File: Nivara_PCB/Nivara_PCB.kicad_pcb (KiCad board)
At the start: 4 copper layers, 102.2 x 83 mm, 14 parts, among them J1 NPN_IN, J10 Analog_Out, J11 RELAY, J2 PNP_IN, J3 D_IN, J4 Analaog_In, J5 RUN/STOP, J6 FUENTE, J7 NPN_OUT, J8 PNP_OUT, J9 RS485, U1 ESP32-S3-WROOM-1

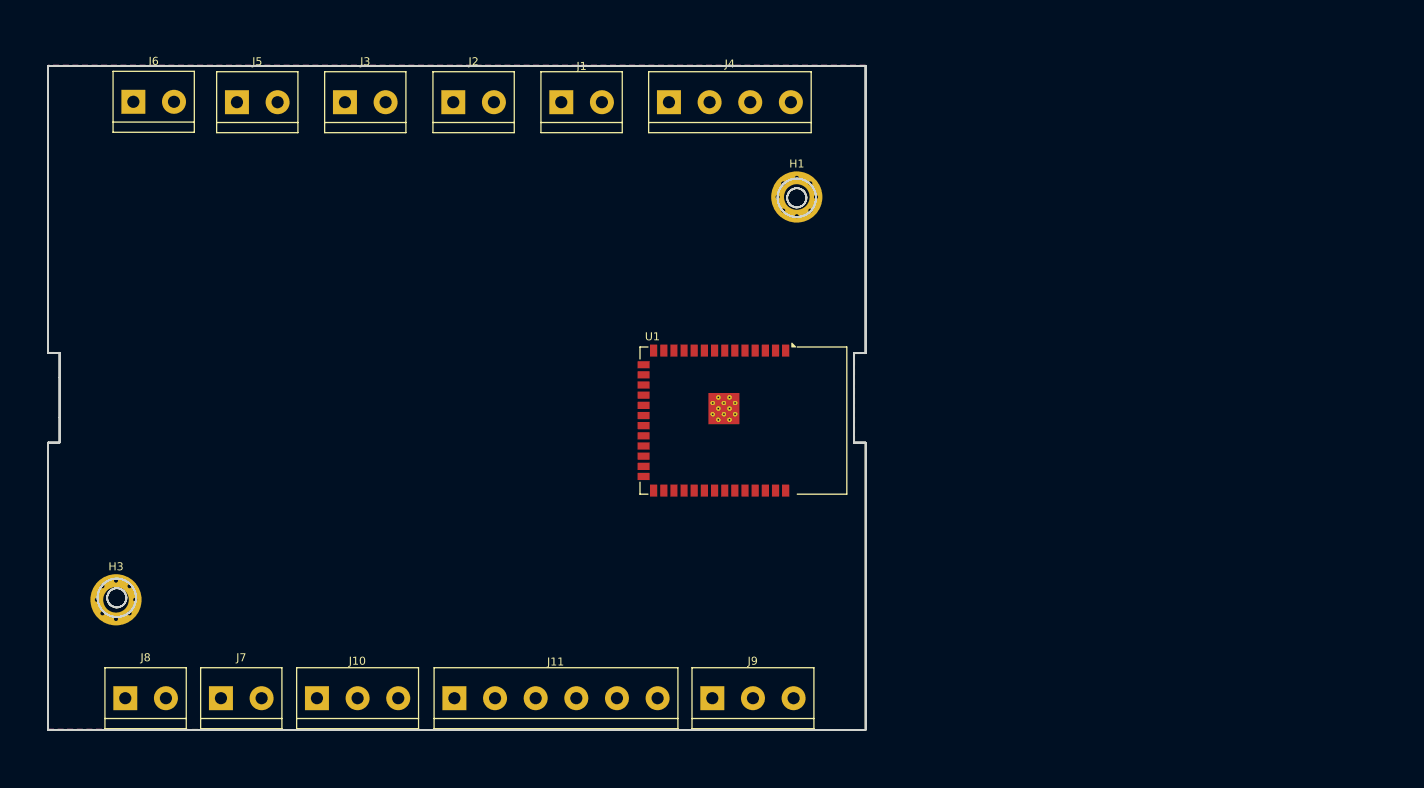
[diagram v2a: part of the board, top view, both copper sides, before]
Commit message: Cambios en el PCB de Nivara. Ruteo de emtradas y salidas NPN y PNP.
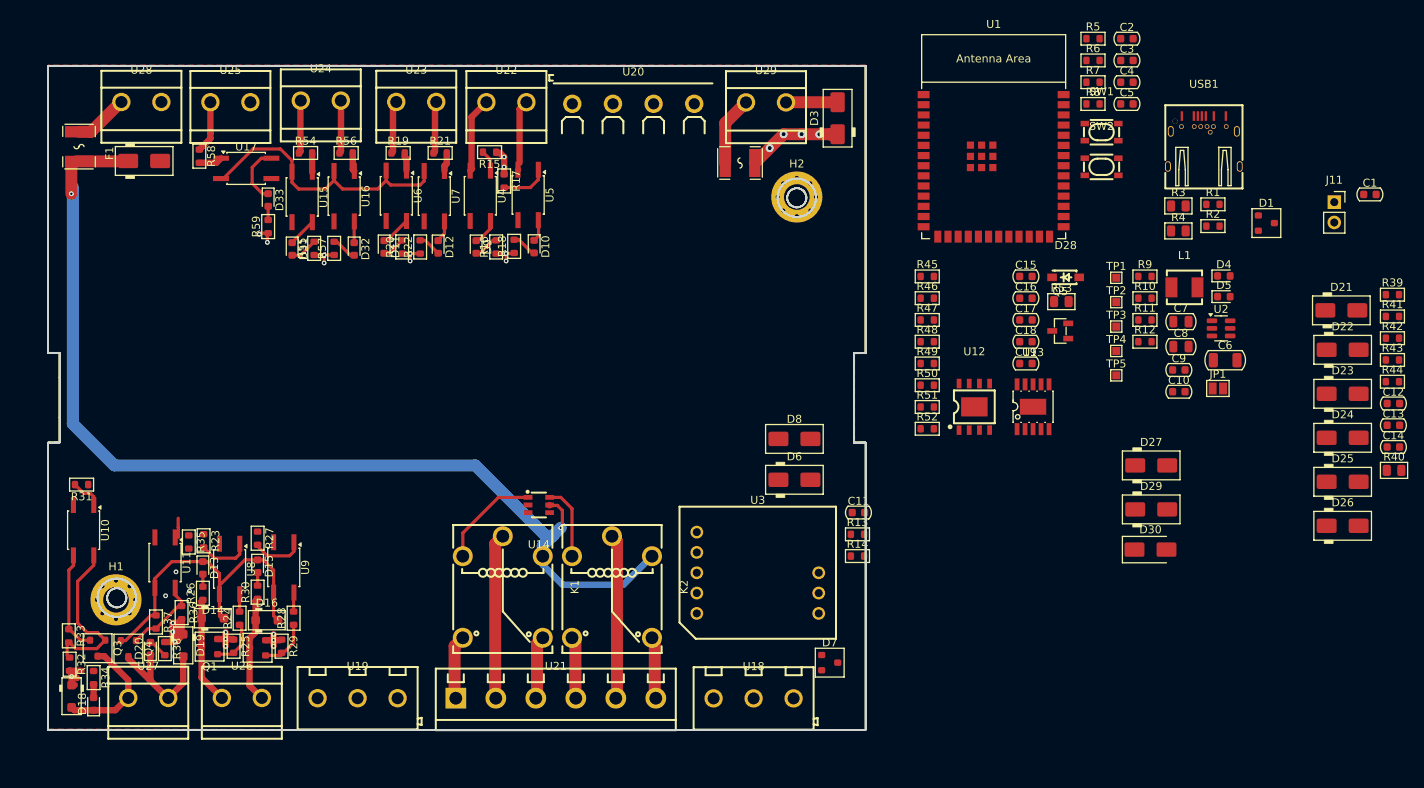
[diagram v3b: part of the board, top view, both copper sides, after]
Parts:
- removed J1: NPN_IN, TerminalBlock:TerminalBlock_bornier-2_P5.08mm
- removed J10: Analog_Out, TerminalBlock:TerminalBlock_bornier-3_P5.08mm
- removed J2: PNP_IN, TerminalBlock:TerminalBlock_bornier-2_P5.08mm
- removed J3: D_IN, TerminalBlock:TerminalBlock_bornier-2_P5.08mm
- removed J4: Analaog_In, TerminalBlock:TerminalBlock_bornier-4_P5.08mm
- removed J5: RUN/STOP, TerminalBlock:TerminalBlock_bornier-2_P5.08mm
- removed J6: FUENTE, TerminalBlock:TerminalBlock_bornier-2_P5.08mm
- removed J7: NPN_OUT, TerminalBlock:TerminalBlock_bornier-2_P5.08mm
- removed J8: PNP_OUT, TerminalBlock:TerminalBlock_bornier-2_P5.08mm
- removed J9: RS485, TerminalBlock:TerminalBlock_bornier-3_P5.08mm
- added C1: 100nF, PCM_Capacitor_SMD_AKL:C_0603_1608Metric, F.Cu at (263.5, 61.0)
- added C10: 22uF, PCM_Capacitor_SMD_AKL:C_0603_1608Metric, F.Cu at (239.7, 85.7)
- added C11: 10uF, PCM_Capacitor_SMD_AKL:C_0603_1608Metric, F.Cu at (199.6, 100.8)
- added C12: 10nF, PCM_Capacitor_SMD_AKL:C_0603_1608Metric, F.Cu at (266.5, 87.2)
- added C13: 100nF, PCM_Capacitor_SMD_AKL:C_0603_1608Metric, F.Cu at (266.5, 89.9)
- added C14: 100nF, PCM_Capacitor_SMD_AKL:C_0603_1608Metric, F.Cu at (266.5, 92.6)
- added C15: 0.1uF, PCM_Capacitor_SMD_AKL:C_0603_1608Metric, F.Cu at (220.5, 71.3)
- added C16: 1uF, PCM_Capacitor_SMD_AKL:C_0603_1608Metric, F.Cu at (220.5, 74.0)
- added C17: 220pF, PCM_Capacitor_SMD_AKL:C_0603_1608Metric, F.Cu at (220.5, 76.7)
- added C18: 1uF, PCM_Capacitor_SMD_AKL:C_0603_1608Metric, F.Cu at (220.5, 79.4)
- added C19: 0.1uF, PCM_Capacitor_SMD_AKL:C_0603_1608Metric, F.Cu at (220.5, 82.2)
- added C2: 22uF, PCM_Capacitor_SMD_AKL:C_0603_1608Metric, F.Cu at (233.2, 41.6)
- added C3: 1uF, PCM_Capacitor_SMD_AKL:C_0603_1608Metric, F.Cu at (233.2, 44.3)
- added C4: 100nF, PCM_Capacitor_SMD_AKL:C_0603_1608Metric, F.Cu at (233.2, 47.0)
- added C5: 1uF, PCM_Capacitor_SMD_AKL:C_0603_1608Metric, F.Cu at (233.2, 49.7)
- added C6: 10uF, PCM_Capacitor_SMD_AKL:C_1206_3216Metric, F.Cu at (245.4, 81.8)
- added C7: 100nF, PCM_Capacitor_SMD_AKL:C_0805_2012Metric, F.Cu at (239.9, 76.9)
- added C8: 100pF, PCM_Capacitor_SMD_AKL:C_0805_2012Metric, F.Cu at (239.9, 80.0)
- added C9: 22uF, PCM_Capacitor_SMD_AKL:C_0603_1608Metric, F.Cu at (239.7, 83.0)
- added D1: SM712, PCM_Package_TO_SOT_SMD_AKL:SOT-23, F.Cu at (250.6, 64.6)
- added D10: LED ON, LED_SMD:LED_0603_1608Metric, F.Cu at (159.1, 67.6)
- added D11: LED ON, LED_SMD:LED_0603_1608Metric, F.Cu at (140.3, 67.6)
- added D12: LED ON, LED_SMD:LED_0603_1608Metric, F.Cu at (147.1, 67.6)
- added D13: LED ON, LED_SMD:LED_0603_1608Metric, F.Cu at (117.7, 107.7)
- added D14: PMEG4010CEH, PCM_Diode_SMD_AKL:D_SOD-123F, F.Cu at (118.9, 114.0)
- added D15: LED ON, LED_SMD:LED_0603_1608Metric, F.Cu at (124.5, 107.5)
- added D16: PMEG4010CEH, PCM_Diode_SMD_AKL:D_SOD-123F, F.Cu at (125.7, 114.2)
- added D17: PMEG4010CEH, PCM_Diode_SMD_AKL:D_SOD-123F, F.Cu at (101.2, 123.8)
- added D18: LED ON, LED_SMD:LED_0603_1608Metric, F.Cu at (104.0, 124.7)
- added D19: PMEG4010CEH, PCM_Diode_SMD_AKL:D_SOD-123F, F.Cu at (115.2, 117.4)
- added D2: SMAJ33A, PCM_Diode_SMD_AKL:D_SMA, F.Cu at (110.3, 56.8)
- added D20: LED ON, LED_SMD:LED_0603_1608Metric, F.Cu at (111.1, 117.8)
- added D21: SMAJ5.0A, PCM_Diode_SMD_AKL:D_SMA, F.Cu at (260.0, 75.5)
- added D22: SMAJ5.0A, PCM_Diode_SMD_AKL:D_SMA, F.Cu at (260.1, 80.4)
- added D23: SMAJ5.0A, PCM_Diode_SMD_AKL:D_SMA, F.Cu at (260.1, 85.9)
- added D24: SMAJ5.0A, PCM_Diode_SMD_AKL:D_SMA, F.Cu at (260.1, 91.4)
- added D25: SMAJ5.0A, PCM_Diode_SMD_AKL:D_SMA, F.Cu at (260.1, 96.9)
- added D26: SMAJ5.0A, PCM_Diode_SMD_AKL:D_SMA, F.Cu at (260.1, 102.4)
- added D27: SMAJ12A, PCM_Diode_SMD_AKL:D_SMA, F.Cu at (236.2, 94.9)
- added D28: BZT52C12_C2891780, EasyEDA:SOD-123_L2.7-W1.6-LS3.7-RD-1, F.Cu at (225.5, 71.4)
- added D29: SMAJ33A, PCM_Diode_SMD_AKL:D_SMA, F.Cu at (236.2, 100.4)
- added D3: SMAJ33A, PCM_Diode_SMD_AKL:D_SMA, F.Cu at (197.0, 51.5)
- added D30: MRA4007T3G, Diode_SMD:D_SMA, F.Cu at (236.1, 105.4)
- added D31: LED ON, LED_SMD:LED_0603_1608Metric, F.Cu at (128.8, 67.8)
- added D32: LED ON, LED_SMD:LED_0603_1608Metric, F.Cu at (136.6, 67.8)
- added D33: LED ON, LED_SMD:LED_0603_1608Metric, F.Cu at (125.8, 61.7)
- added D4: LED ON, LED_SMD:LED_0603_1608Metric, F.Cu at (245.3, 71.2)
- added D5: LED 3.3V, LED_SMD:LED_0603_1608Metric, F.Cu at (245.3, 73.8)
- added D6: SMAJ5.0A, PCM_Diode_SMD_AKL:D_SMA, F.Cu at (191.6, 96.7)
- added D7: SM712, PCM_Package_TO_SOT_SMD_AKL:SOT-23, F.Cu at (196.0, 119.6)
- added D8: SMAJ12CA, PCM_Diode_SMD_AKL:D_SMA_TVS, F.Cu at (191.6, 91.6)
- added D9: LED ON, LED_SMD:LED_0603_1608Metric, F.Cu at (151.8, 67.6)
- added F1: BSMD1812-150-33V, EasyEDA:F1812, F.Cu at (102.2, 55.0)
- added F2: BSMD1812-150-33V, EasyEDA:F1812, F.Cu at (184.8, 57.1)
- added JP1: SolderJumper_2_Open, Jumper:SolderJumper-2_P1.3mm_Open_Pad1.0x1.5mm, F.Cu at (244.5, 85.3)
- added K1: SRA-24VDC-CL, EasyEDA:RELAY-TH_SRA-X-CX, F.Cu at (155.2, 110.1)
- added K2: SRA-24VDC-CL, EasyEDA:RELAY-TH_SRA-X-CX, F.Cu at (168.8, 110.1)
- added L1: CXP0420-6R8M-AG(6.8UH), EasyEDA:IND-SMD_L4.4-W4.2_CXP0420, F.Cu at (240.4, 72.6)
- added Q1: AO3407A, PCM_Package_TO_SOT_SMD_AKL:SOT-23, F.Cu at (118.5, 117.5)
- added Q2: AO3407A, PCM_Package_TO_SOT_SMD_AKL:SOT-23, F.Cu at (124.5, 117.7)
- added Q3: IRLML0040, PCM_Package_TO_SOT_SMD_AKL:SOT-23, F.Cu at (104.5, 117.8)
- added Q4: IRLML0040, PCM_Package_TO_SOT_SMD_AKL:SOT-23, F.Cu at (108.3, 117.8)
- added Q5: IRLML6402TRPBF-JSM, EasyEDA:SOT-23-3_L2.9-W1.3-P1.90-LS2.4-BR, F.Cu at (224.8, 78.1)
- added R1: 14k, PCM_Resistor_SMD_AKL:R_0603_1608Metric, F.Cu at (243.9, 62.3)
- added R10: 196k, PCM_Resistor_SMD_AKL:R_0603_1608Metric, F.Cu at (235.4, 74.0)
- added R11: 62k, PCM_Resistor_SMD_AKL:R_0603_1608Metric, F.Cu at (235.4, 76.7)
- added R12: 100, PCM_Resistor_SMD_AKL:R_0603_1608Metric, F.Cu at (235.4, 79.4)
- added R13: R_0603, PCM_Resistor_SMD_AKL:R_0603_1608Metric, F.Cu at (199.5, 103.5)
- added R14: R_0603, PCM_Resistor_SMD_AKL:R_0603_1608Metric, F.Cu at (199.5, 106.2)
- added R15: 1k, PCM_Resistor_SMD_AKL:R_0603_1608Metric, F.Cu at (153.5, 55.7)
- added R16: 140, PCM_Resistor_SMD_AKL:R_0603_1608Metric, F.Cu at (154.3, 67.6)
- added R17: 1k, PCM_Resistor_SMD_AKL:R_0603_1608Metric, F.Cu at (155.3, 59.3)
- added R18: 140, PCM_Resistor_SMD_AKL:R_0603_1608Metric, F.Cu at (156.6, 67.5)
- added R19: 1k, PCM_Resistor_SMD_AKL:R_0603_1608Metric, F.Cu at (142.1, 55.8)
- added R2: 10k, PCM_Resistor_SMD_AKL:R_0603_1608Metric, F.Cu at (243.9, 65.0)
- added R20: 140, PCM_Resistor_SMD_AKL:R_0603_1608Metric, F.Cu at (142.6, 67.6)
- added R21: 1k, PCM_Resistor_SMD_AKL:R_0603_1608Metric, F.Cu at (147.3, 55.8)
- added R22: 140, PCM_Resistor_SMD_AKL:R_0603_1608Metric, F.Cu at (144.8, 67.6)
- added R23: 100, PCM_Resistor_SMD_AKL:R_0603_1608Metric, F.Cu at (117.8, 104.3)
- added R24: 100, PCM_Resistor_SMD_AKL:R_0603_1608Metric, F.Cu at (122.2, 114.0)
- added R25: 100k, PCM_Resistor_SMD_AKL:R_0603_1608Metric, F.Cu at (121.5, 117.5)
- added R26: 1.5k, PCM_Resistor_SMD_AKL:R_0603_1608Metric, F.Cu at (117.7, 110.9)
- added R27: 100, PCM_Resistor_SMD_AKL:R_0603_1608Metric, F.Cu at (124.5, 104.0)
- added R28: 100, PCM_Resistor_SMD_AKL:R_0603_1608Metric, F.Cu at (129.0, 114.0)
- added R29: 100k, PCM_Resistor_SMD_AKL:R_0603_1608Metric, F.Cu at (127.5, 117.5)
- added R3: 5.1k, PCM_Resistor_SMD_AKL:R_0805_2012Metric, F.Cu at (239.6, 62.5)
- added R30: 1.5k, PCM_Resistor_SMD_AKL:R_0603_1608Metric, F.Cu at (124.5, 110.8)
- added R31: 100, PCM_Resistor_SMD_AKL:R_0603_1608Metric, F.Cu at (102.5, 97.3)
- added R32: 30k, PCM_Resistor_SMD_AKL:R_0603_1608Metric, F.Cu at (101.0, 119.8)
- added R33: 22k, PCM_Resistor_SMD_AKL:R_0603_1608Metric, F.Cu at (100.9, 116.2)
- added R34: 1.5k, PCM_Resistor_SMD_AKL:R_0603_1608Metric, F.Cu at (104.0, 121.4)
- added R35: 100, PCM_Resistor_SMD_AKL:R_0603_1608Metric, F.Cu at (115.9, 104.5)
- added R36: 30k, PCM_Resistor_SMD_AKL:R_0603_1608Metric, F.Cu at (115.0, 113.3)
- added R37: 22k, PCM_Resistor_SMD_AKL:R_0603_1608Metric, F.Cu at (111.8, 114.5)
- added R38: 1.5k, PCM_Resistor_SMD_AKL:R_0603_1608Metric, F.Cu at (112.9, 117.8)
- added R39: 1k, PCM_Resistor_SMD_AKL:R_0603_1608Metric, F.Cu at (266.4, 73.6)
- added R4: 5.1k, PCM_Resistor_SMD_AKL:R_0805_2012Metric, F.Cu at (239.6, 65.6)
- added R40: 145, PCM_Resistor_SMD_AKL:R_0805_2012Metric, F.Cu at (266.6, 95.5)
- added R41: 100k, PCM_Resistor_SMD_AKL:R_0603_1608Metric, F.Cu at (266.4, 76.3)
- added R42: 10k, PCM_Resistor_SMD_AKL:R_0603_1608Metric, F.Cu at (266.4, 79.0)
- added R43: 24k, PCM_Resistor_SMD_AKL:R_0603_1608Metric, F.Cu at (266.4, 81.7)
- added R44: 10k, PCM_Resistor_SMD_AKL:R_0603_1608Metric, F.Cu at (266.4, 84.4)
- added R45: 4K7, PCM_Resistor_SMD_AKL:R_0603_1608Metric, F.Cu at (208.2, 71.3)
- added R46: 4K7, PCM_Resistor_SMD_AKL:R_0603_1608Metric, F.Cu at (208.2, 74.0)
- added R47: 0, PCM_Resistor_SMD_AKL:R_0603_1608Metric, F.Cu at (208.2, 76.7)
- added R48: 10K, PCM_Resistor_SMD_AKL:R_0603_1608Metric, F.Cu at (208.2, 79.4)
- added R49: 4K7, PCM_Resistor_SMD_AKL:R_0603_1608Metric, F.Cu at (208.2, 82.2)
- added R5: 10k, PCM_Resistor_SMD_AKL:R_0603_1608Metric, F.Cu at (228.9, 41.6)
- added R50: 4K7, PCM_Resistor_SMD_AKL:R_0603_1608Metric, F.Cu at (208.2, 84.9)
- added R51: 2.5k, PCM_Resistor_SMD_AKL:R_0603_1608Metric, F.Cu at (208.2, 87.6)
- added R52: 100k, PCM_Resistor_SMD_AKL:R_0603_1608Metric, F.Cu at (208.2, 90.3)
- added R53: 15, PCM_Resistor_SMD_AKL:R_0805_2012Metric, F.Cu at (225.0, 74.4)
- added R54: 1k, PCM_Resistor_SMD_AKL:R_0603_1608Metric, F.Cu at (130.5, 55.8)
- added R55: 140, PCM_Resistor_SMD_AKL:R_0603_1608Metric, F.Cu at (131.6, 67.8)
- added R56: 1k, PCM_Resistor_SMD_AKL:R_0603_1608Metric, F.Cu at (135.6, 55.8)
- added R57: 140, PCM_Resistor_SMD_AKL:R_0603_1608Metric, F.Cu at (134.1, 67.8)
- added R58: 1k, PCM_Resistor_SMD_AKL:R_0603_1608Metric, F.Cu at (117.2, 56.2)
- added R59: 140, PCM_Resistor_SMD_AKL:R_0603_1608Metric, F.Cu at (125.8, 65.0)
- added R6: 220, PCM_Resistor_SMD_AKL:R_0603_1608Metric, F.Cu at (228.9, 44.3)
- added R7: 220, PCM_Resistor_SMD_AKL:R_0603_1608Metric, F.Cu at (228.9, 47.0)
- added R8: 10k, PCM_Resistor_SMD_AKL:R_0603_1608Metric, F.Cu at (228.9, 49.7)
- added R9: 1k2, PCM_Resistor_SMD_AKL:R_0603_1608Metric, F.Cu at (235.4, 71.3)
- added SW1: SKRPACE010, EasyEDA:KEY-SMD_4P-L4.2-W3.2-P2.20-LS4.6, F.Cu at (230.0, 53.2)
- added SW2: SKRPACE010, EasyEDA:KEY-SMD_4P-L4.2-W3.2-P2.20-LS4.6, F.Cu at (230.0, 57.6)
- added TP1: +VCC1, TestPoint:TestPoint_Pad_1.0x1.0mm, F.Cu at (231.8, 71.4)
- added TP2: FB, TestPoint:TestPoint_Pad_1.0x1.0mm, F.Cu at (231.8, 74.5)
- added TP3: GND, TestPoint:TestPoint_Pad_1.0x1.0mm, F.Cu at (231.8, 77.5)
- added TP4: +3.3V, TestPoint:TestPoint_Pad_1.0x1.0mm, F.Cu at (231.8, 80.6)
- added TP5: +3.3Vout, TestPoint:TestPoint_Pad_1.0x1.0mm, F.Cu at (231.8, 83.6)
- added U10: LTV-357T, Package_SO:SO-4_4.4x3.6mm_P2.54mm, F.Cu at (102.8, 103.0)
- added U11: LTV-357T, Package_SO:SO-4_4.4x3.6mm_P2.54mm, F.Cu at (112.9, 107.0)
- added U12: GP8201S-TC50-EW, EasyEDA:ESOP-8_L4.9-W3.9-P1.27-LS6.0-BL-EP, F.Cu at (214.1, 87.6)
- added U13: GP8303-TC50-EW, EasyEDA:ESOP-10_L4.9-W3.9-P1.00-LS6.1-BL-EP, F.Cu at (221.4, 87.6)
- added U14: LK1802, EasyEDA:SOT-23-6_L2.9-W1.6-P0.95-LS2.8-BR, F.Cu at (159.7, 99.8)
- added U15: LTV-357T, Package_SO:SO-4_4.4x3.6mm_P2.54mm, F.Cu at (130.1, 61.3)
- added U16: LTV-357T, Package_SO:SO-4_4.4x3.6mm_P2.54mm, F.Cu at (135.3, 61.2)
- added U17: LTV-357T, Package_SO:SO-4_4.4x3.6mm_P2.54mm, F.Cu at (123.1, 57.8)
- added U18: RS485, EasyEDA:CONN-TH_XY126V-5.0-3P, F.Cu at (186.5, 124.0)
- added U19: ANALOG_OUT., EasyEDA:CONN-TH_XY126V-5.0-3P, F.Cu at (137.0, 124.0)
- added U2: AP63200WU, Package_TO_SOT_SMD:TSOT-23-6, F.Cu at (244.9, 77.8)
- added U20: ANALOG_IN, EasyEDA:CONN-TH_4P-P5.00_DIBO_DB126V-5.0-4P-GN-P, F.Cu at (171.5, 49.7)
- added U21: RELAY, EasyEDA:CONN-TH_DB126V-5.0-6P-GN, F.Cu at (161.8, 124.0)
- added U22: NPN_IN, EasyEDA:CONN-TH_XY126V-5.0-2P, F.Cu at (155.6, 49.5)
- added U23: PNP_IN, EasyEDA:CONN-TH_XY126V-5.0-2P, F.Cu at (144.3, 49.5)
- added U24: D_IN, EasyEDA:CONN-TH_XY126V-5.0-2P, F.Cu at (132.4, 49.3)
- added U25: RUN/STOP, EasyEDA:CONN-TH_XY126V-5.0-2P, F.Cu at (121.1, 49.5)
- added U26: NPN_OUT, EasyEDA:CONN-TH_XY126V-5.0-2P, F.Cu at (122.5, 124.0)
- added U27: PNP_OUT, EasyEDA:CONN-TH_XY126V-5.0-2P, F.Cu at (110.8, 124.0)
- added U28: FUENTE IN, EasyEDA:CONN-TH_XY126V-5.0-2P, F.Cu at (110.0, 49.5)
- added U29: FUENTE EX, EasyEDA:CONN-TH_XY126V-5.0-2P, F.Cu at (188.1, 49.5)
- added U3: RSM3485ECHT_C2992406, EasyEDA:COMM-TH_8P-L19.5-W16.5-P2.54-BL, F.Cu at (187.0, 108.3)
- added U4: LTV-357T, Package_SO:SO-4_4.4x3.6mm_P2.54mm, F.Cu at (152.3, 61.2)
- added U5: LTV-357T, Package_SO:SO-4_4.4x3.6mm_P2.54mm, F.Cu at (158.3, 61.1)
- added U6: LTV-357T, Package_SO:SO-4_4.4x3.6mm_P2.54mm, F.Cu at (141.8, 61.2)
- added U7: LTV-357T, Package_SO:SO-4_4.4x3.6mm_P2.54mm, F.Cu at (146.6, 61.2)
- added U8: LTV-357T, Package_SO:SO-4_4.4x3.6mm_P2.54mm, F.Cu at (121.0, 107.8)
- added U9: LTV-357T, Package_SO:SO-4_4.4x3.6mm_P2.54mm, F.Cu at (127.8, 107.7)
- added USB1: USB-306B, EasyEDA:USB-TYPE-C-TH_USB-306B, F.Cu at (242.8, 54.4)
- J11: value RELAY -> PINHD_1x2_Female; footprint TerminalBlock:TerminalBlock_bornier-6_P5.08mm -> Connector_PinSocket_2.54mm:PinSocket_1x02_P2.54mm_Vertical
- U1: footprint RF_Module:ESP32-S3-WROOM-1 -> PCM_Espressif:ESP32-S3-WROOM-1
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- renumbered H3 to H1, H1 to H2
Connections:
- net GND renamed GND1
- J11 pad 1: /NIVARA_BOARD/RLY_1_NC -> /NIVARA_BOARD/AUX_1
- J11 pad 2: /NIVARA_BOARD/RLY_1_C -> /NIVARA_BOARD/AUX_2
- U1 pad 13: unconnected-(U1-USB_D--Pad13) -> /NIVARA_BOARD/USB_D-
- U1 pad 14: unconnected-(U1-USB_D+-Pad14) -> /NIVARA_BOARD/USB_D+
- U1 pad 18: unconnected-(U1-IO10-Pad18) -> /NIVARA_BOARD/ANALOG_OUT/ESP_SEL_VOUT
- U1 pad 19: unconnected-(U1-IO11-Pad19) -> /NIVARA_BOARD/ANALOG_OUT/SCLK_V
- U1 pad 20: unconnected-(U1-IO12-Pad20) -> /NIVARA_BOARD/ANALOG_OUT/SDA_V
- U1 pad 21: unconnected-(U1-IO13-Pad21) -> /NIVARA_BOARD/ANALOG_OUT/SCLK_C
- U1 pad 22: unconnected-(U1-IO14-Pad22) -> /NIVARA_BOARD/ANALOG_OUT/SDA_C
- U1 pad 23: unconnected-(U1-IO21-Pad23) -> /NIVARA_BOARD/PNP_OUT/ESP_PNP_OUT_1
- U1 pad 24: unconnected-(U1-IO47-Pad24) -> /NIVARA_BOARD/PNP_OUT/ESP_PNP_OUT_2
- U1 pad 25: unconnected-(U1-IO48-Pad25) -> Net-(U1-GPIO48/SPICLK_N/SUBSPICLK_N_DIFF)
- U1 pad 26: unconnected-(U1-IO45-Pad26) -> Net-(U1-GPIO45)
- U1 pad 27: unconnected-(U1-IO0-Pad27) -> Net-(U1-GPIO0/BOOT)
- U1 pad 28: unconnected-(U1-IO35-Pad28) -> /NIVARA_BOARD/D_IN/ESP_D_IN_1
- U1 pad 29: unconnected-(U1-IO36-Pad29) -> /NIVARA_BOARD/D_IN/ESP_D_IN_2
- U1 pad 30: unconnected-(U1-IO37-Pad30) -> /NIVARA_BOARD/D_IN/ESP_RUN_IN
- U1 pad 32: unconnected-(U1-IO39-Pad32) -> /NIVARA_BOARD/NPN_IN/ESP_NPN_IN_1
- U1 pad 33: unconnected-(U1-IO40-Pad33) -> /NIVARA_BOARD/NPN_IN/ESP_NPN_IN_2
- U1 pad 34: unconnected-(U1-IO41-Pad34) -> /NIVARA_BOARD/NPN_OUT/ESP_NPN_OUT_1
- U1 pad 35: unconnected-(U1-IO42-Pad35) -> /NIVARA_BOARD/NPN_OUT/ESP_NPN_OUT_2
- U1 pad 38: unconnected-(U1-IO2-Pad38) -> /NIVARA_BOARD/RELAY1&2/ESP_RY1
- U1 pad 39: unconnected-(U1-IO1-Pad39) -> /NIVARA_BOARD/RELAY1&2/ESP_RLY2
- U1 pad 4: unconnected-(U1-IO4-Pad4) -> /NIVARA_BOARD/ANALOG_IN/ESP_4-20_IN
- U1 pad 5: unconnected-(U1-IO5-Pad5) -> /NIVARA_BOARD/ANALOG_IN/ESP_A0_32_IN_1
- U1 pad 6: unconnected-(U1-IO6-Pad6) -> /NIVARA_BOARD/ANALOG_IN/ESP_A0_10_IN_1
- U1 pad 7: unconnected-(U1-IO7-Pad7) -> /NIVARA_BOARD/Vbus
- U1 pad 8: unconnected-(U1-IO15-Pad8) -> /NIVARA_BOARD/PNP_IN/ESP_PNP_IN_1
- U1 pad 9: unconnected-(U1-IO16-Pad9) -> /NIVARA_BOARD/PNP_IN/ESP_PNP_IN_2
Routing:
- net VCC1: track 0.00 -> 131.8 mm, vias 0 -> 2
- net GND2: track 0.00 -> 97.4 mm
- net VCC2: track 0.00 -> 37.7 mm, vias 0 -> 16
- net Net-(Q3-G): track 0.00 -> 21.0 mm
- net /NIVARA_BOARD/RLY_1_C: track 0.00 -> 20.7 mm
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- added copper zone on In2.Cu, net +3.3V
- added copper zone on In1.Cu, net VCC2

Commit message: Modificación del PCB.
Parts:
- removed USB1: USB-306B, EasyEDA:USB-TYPE-C-TH_USB-306B
- added U30: GT-USB-7010ASV, EasyEDA:USB-C-SMD_G-SWITCH_GT-USB-7010ASV, F.Cu at (246.2, 51.1)
- moved C11 70.8 mm to (267.4, 121.1)
- moved D7 70.8 mm to (263.8, 139.8)
- moved D6 70.8 mm to (259.4, 117.0)
- moved D8 70.8 mm to (259.4, 111.9)
- moved U3 70.8 mm to (254.8, 128.6)
- moved R13 70.8 mm to (267.3, 123.8)
- moved R14 70.8 mm to (267.3, 126.5)
- moved K1 0.65 mm to (154.5, 110.1)
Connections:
- D1 pad 1: /NIVARA_BOARD/USB_D- -> /NIVARA_BOARD/USB_D+
- D1 pad 2: /NIVARA_BOARD/USB_D+ -> /NIVARA_BOARD/USB_D-
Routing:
- net GND2: track 97.4 -> 9.98 mm, vias 0 -> 18
- net +3.3V: track 12.1 -> 0.00 mm, vias 8 -> 0
- net GND1: track 0.00 -> 11.8 mm, vias 3 -> 18
- net VCC1: track 131.8 -> 132.4 mm
- net VCC2: track 37.7 -> 37.5 mm, vias 16 -> 17
- added copper zone on F.Cu, net +3.3V
- added copper zone on In1.Cu, net GND1
- added copper zone on B.Cu, net GND2
- added copper zone on In2.Cu, net VCC2
- removed copper zone on In2.Cu, net +3.3V
- removed copper zone on B.Cu, net GND1
- removed copper zone on F.Cu, net GND1
- removed copper zone on In1.Cu, net VCC2

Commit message: Cambios realizados en el PCB y el esquema de Nivara_PCB.
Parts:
- removed F2: BSMD1812-150-33V, EasyEDA:F1812
- removed J11: PINHD_1x2_Female, Connector_PinSocket_2.54mm:PinSocket_1x02_P2.54mm_Vertical
- removed R56, R58: 1k, PCM_Resistor_SMD_AKL:R_0603_1608Metric
- removed R57, R59: 140, PCM_Resistor_SMD_AKL:R_0603_1608Metric
- removed U20: ANALOG_IN, EasyEDA:CONN-TH_4P-P5.00_DIBO_DB126V-5.0-4P-GN-P
- removed U21: RELAY, EasyEDA:CONN-TH_DB126V-5.0-6P-GN
- removed U22: NPN_IN, EasyEDA:CONN-TH_XY126V-5.0-2P
- removed U23: PNP_IN, EasyEDA:CONN-TH_XY126V-5.0-2P
- removed U24: D_IN, EasyEDA:CONN-TH_XY126V-5.0-2P
- removed U25: RUN/STOP, EasyEDA:CONN-TH_XY126V-5.0-2P
- removed U26: NPN_OUT, EasyEDA:CONN-TH_XY126V-5.0-2P
- removed U27: PNP_OUT, EasyEDA:CONN-TH_XY126V-5.0-2P
- removed U28: FUENTE IN, EasyEDA:CONN-TH_XY126V-5.0-2P
- removed U29: FUENTE EX, EasyEDA:CONN-TH_XY126V-5.0-2P
- removed U30: GT-USB-7010ASV, EasyEDA:USB-C-SMD_G-SWITCH_GT-USB-7010ASV
- added CN1: ANALOG_IN, EasyEDA:CONN-TH_DB128V-5.0-4P, F.Cu at (161.0, 105.2)
- added CN2: RELAY, EasyEDA:CONN-TH_DB126V-5.0-6P-GN, F.Cu at (165.3, 95.0)
- added D34: SMAJ5.0A, PCM_Diode_SMD_AKL:D_SMA, F.Cu at (141.6, 267.6)
- added D35: BZT52C12_C2891780, EasyEDA:SOD-123_L2.7-W1.6-LS3.7-RD-1, F.Cu at (120.9, 316.7)
- added D36: SMAJ33A, PCM_Diode_SMD_AKL:D_SMA, F.Cu at (113.9, 310.6)
- added D37: MRA4007T3G, Diode_SMD:D_SMA, F.Cu at (113.8, 315.7)
- added J1: AUXILIAR, Connector_PinSocket_2.54mm:PinSocket_1x02_P2.54mm_Vertical, F.Cu at (168.6, 84.7)
- added P1: NPN_IN, EasyEDA:CONN-TH_XY126V-5.0-2P, F.Cu at (132.8, 72.7)
- added P2: PNP_IN, EasyEDA:CONN-TH_XY126V-5.0-2P, F.Cu at (132.8, 83.0)
- added P3: D_IN, EasyEDA:CONN-TH_XY126V-5.0-2P, F.Cu at (132.8, 93.3)
- added P4: RUN/STOP, EasyEDA:CONN-TH_XY126V-5.0-2P, F.Cu at (132.8, 103.6)
- added P5: NPN_OUT, EasyEDA:CONN-TH_XY126V-5.0-2P, F.Cu at (144.1, 72.7)
- added P6: PNP_OUT, EasyEDA:CONN-TH_XY126V-5.0-2P, F.Cu at (144.1, 83.0)
- added P7: RS485, EasyEDA:CONN-TH_3P-P5.00_WJ500V-5.08-3P, F.Cu at (112.0, 123.0)
- added P8: ANALOG_OUT., EasyEDA:CONN-TH_3P-P5.00_WJ500V-5.08-3P, F.Cu at (128.0, 123.0)
- C10: value 22uF -> 10nF
- C11: value 10uF -> 0.1uF
- C12: value 10nF -> 1uF
- C15: value 0.1uF -> 1uF
- C3: value 1uF -> 100nF
- C4: value 100nF -> 10uF; footprint PCM_Capacitor_SMD_AKL:C_0603_1608Metric -> PCM_Capacitor_SMD_AKL:C_1206_3216Metric
- C5: value 1uF -> 100nF; footprint PCM_Capacitor_SMD_AKL:C_0603_1608Metric -> PCM_Capacitor_SMD_AKL:C_0805_2012Metric
- C6: value 10uF -> 100pF; footprint PCM_Capacitor_SMD_AKL:C_1206_3216Metric -> PCM_Capacitor_SMD_AKL:C_0805_2012Metric
- C7: value 100nF -> 22uF; footprint PCM_Capacitor_SMD_AKL:C_0805_2012Metric -> PCM_Capacitor_SMD_AKL:C_0603_1608Metric
- C8: value 100pF -> 22uF; footprint PCM_Capacitor_SMD_AKL:C_0805_2012Metric -> PCM_Capacitor_SMD_AKL:C_0603_1608Metric
- C9: value 22uF -> 10uF
- D1: value SM712 -> SS12; footprint PCM_Package_TO_SOT_SMD_AKL:SOT-23 -> PCM_Diode_SMD_AKL:D_SMA
- D12, D13, D15, D9: value LED ON -> PMEG4010CEH; footprint LED_SMD:LED_0603_1608Metric -> PCM_Diode_SMD_AKL:D_SOD-123F
- D14, D16: value PMEG4010CEH -> LED ON; footprint PCM_Diode_SMD_AKL:D_SOD-123F -> LED_SMD:LED_0603_1608Metric
- D17: value PMEG4010CEH -> SMAJ5.0A; footprint PCM_Diode_SMD_AKL:D_SOD-123F -> PCM_Diode_SMD_AKL:D_SMA
- D18, D31, D32, D33: value LED ON -> SMAJ5.0A; footprint LED_SMD:LED_0603_1608Metric -> PCM_Diode_SMD_AKL:D_SMA
- D19: value PMEG4010CEH -> SMAJ12A; footprint PCM_Diode_SMD_AKL:D_SOD-123F -> PCM_Diode_SMD_AKL:D_SMA
- D2: value SMAJ33A -> SM712; footprint PCM_Diode_SMD_AKL:D_SMA -> PCM_Package_TO_SOT_SMD_AKL:SOT-23
- D21, D22, D24: value SMAJ5.0A -> PMEG4010CEH; footprint PCM_Diode_SMD_AKL:D_SMA -> PCM_Diode_SMD_AKL:D_SOD-123F
- D23, D25, D26: value SMAJ5.0A -> LED ON; footprint PCM_Diode_SMD_AKL:D_SMA -> LED_SMD:LED_0603_1608Metric
- D27: value SMAJ12A -> PMEG4010CEH; footprint PCM_Diode_SMD_AKL:D_SMA -> PCM_Diode_SMD_AKL:D_SOD-123F
- D28: value BZT52C12_C2891780 -> LED ON; footprint EasyEDA:SOD-123_L2.7-W1.6-LS3.7-RD-1 -> LED_SMD:LED_0603_1608Metric
- D29: value SMAJ33A -> LED ON; footprint PCM_Diode_SMD_AKL:D_SMA -> LED_SMD:LED_0603_1608Metric
- D30: value MRA4007T3G -> LED ON; footprint Diode_SMD:D_SMA -> LED_SMD:LED_0603_1608Metric
- Q1: value AO3407A -> IRLML0040
- Q4: value IRLML0040 -> AO3407A
- R1: value 14k -> 220
- R10: value 196k -> 140
- R11: value 62k -> 1k
- R12, R28: value 100 -> 140
- R13: value R_0603 -> 100
- R14: value R_0603 -> 22k
- R15: value 1k -> 20k
- R16, R20: value 140 -> 1.5k
- R17: value 1k -> 100
- R18: value 140 -> 100
- R19, R39, R54: value 1k -> 100k
- R2: value 10k -> 220
- R22: value 140 -> 145; footprint PCM_Resistor_SMD_AKL:R_0603_1608Metric -> PCM_Resistor_SMD_AKL:R_0805_2012Metric
- R23, R24: value 100 -> 4K7
- R25: value 100k -> 0
- R26: value 1.5k -> 10K
- R27, R35: value 100 -> 1k
- R29: value 100k -> 100
- R3: value 5.1k -> 1k2; footprint PCM_Resistor_SMD_AKL:R_0805_2012Metric -> PCM_Resistor_SMD_AKL:R_0603_1608Metric
- R30: value 1.5k -> 22k
- R31: value 100 -> 20k
- R32: value 30k -> 1.5k
- R33: value 22k -> 1k
- R34: value 1.5k -> 140
- R36: value 30k -> 140
- R37: value 22k -> 100
- R38: value 1.5k -> 100
- R4: value 5.1k -> 196k; footprint PCM_Resistor_SMD_AKL:R_0805_2012Metric -> PCM_Resistor_SMD_AKL:R_0603_1608Metric
- R40: value 145 -> 1.5k; footprint PCM_Resistor_SMD_AKL:R_0805_2012Metric -> PCM_Resistor_SMD_AKL:R_0603_1608Metric
- R41: value 100k -> 1k
- R42, R44: value 10k -> 140
- R43: value 24k -> 1k
- R45: value 4K7 -> 100k
- R46, R49, R50: value 4K7 -> 10k
- R47: value 0 -> 24k
- R48: value 10K -> 10k
- R5: value 10k -> 62k
- R51: value 2.5k -> 4K7
- R52: value 100k -> 4K7
- R53: value 15 -> 2.5k; footprint PCM_Resistor_SMD_AKL:R_0805_2012Metric -> PCM_Resistor_SMD_AKL:R_0603_1608Metric
- R55: value 140 -> 15; footprint PCM_Resistor_SMD_AKL:R_0603_1608Metric -> PCM_Resistor_SMD_AKL:R_0805_2012Metric
- R6: value 220 -> 100
- R7: value 220 -> R_0603
- R8: value 10k -> R_0603
- R9: value 1k2 -> 1k
- U1: value ESP32-S3-WROOM-1 -> 2.54-2*2; footprint PCM_Espressif:ESP32-S3-WROOM-1 -> Connector_PinHeader_2.54mm:PinHeader_2x02_P2.54mm_Vertical
- U10: value LTV-357T -> GP8201S-TC50-EW; footprint Package_SO:SO-4_4.4x3.6mm_P2.54mm -> EasyEDA:ESOP-8_L4.9-W3.9-P1.27-LS6.0-BL-EP
- U11: value LTV-357T -> LK1802; footprint Package_SO:SO-4_4.4x3.6mm_P2.54mm -> EasyEDA:SOT-23-6_L2.9-W1.6-P0.95-LS2.8-BR
- U12: value GP8201S-TC50-EW -> LTV-357T; footprint EasyEDA:ESOP-8_L4.9-W3.9-P1.27-LS6.0-BL-EP -> Package_SO:SO-4_4.4x3.6mm_P2.54mm
- U13: value GP8303-TC50-EW -> LTV-357T; footprint EasyEDA:ESOP-10_L4.9-W3.9-P1.00-LS6.1-BL-EP -> Package_SO:SO-4_4.4x3.6mm_P2.54mm
- U14: value LK1802 -> LTV-357T; footprint EasyEDA:SOT-23-6_L2.9-W1.6-P0.95-LS2.8-BR -> Package_SO:SO-4_4.4x3.6mm_P2.54mm
- U18: value RS485 -> LTV-357T; footprint EasyEDA:CONN-TH_XY126V-5.0-3P -> Package_SO:SO-4_4.4x3.6mm_P2.54mm
- U19: value ANALOG_OUT. -> GP8303-TC50-EW; footprint EasyEDA:CONN-TH_XY126V-5.0-3P -> EasyEDA:ESOP-10_L4.9-W3.9-P1.00-LS6.1-BL-EP
- U2: value AP63200WU -> FUENTE IN; footprint Package_TO_SOT_SMD:TSOT-23-6 -> EasyEDA:CONN-TH_XY126V-5.0-2P
- U3: value RSM3485ECHT_C2992406 -> ESP32-S3-WROOM-1; footprint EasyEDA:COMM-TH_8P-L19.5-W16.5-P2.54-BL -> PCM_Espressif:ESP32-S3-WROOM-1
- U4: value LTV-357T -> AP63200WU; footprint Package_SO:SO-4_4.4x3.6mm_P2.54mm -> Package_TO_SOT_SMD:TSOT-23-6
- U5: value LTV-357T -> RSM3485ECHT_C2992406; footprint Package_SO:SO-4_4.4x3.6mm_P2.54mm -> EasyEDA:COMM-TH_8P-L19.5-W16.5-P2.54-BL
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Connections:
- C1 pad 1: Net-(C1-Pad1) -> VCC
- C1 pad 2: GND1 -> GND
- C10 pad 1: Net-(JP1-A) -> /NIVARA_BOARD/4-20mA_IN/ESP_4-20_IN
- C10 pad 2: GND1 -> GND
- C11 pad 1: +3.3V -> /NIVARA_BOARD/A0_V_OUT_1
- C11 pad 2: GND1 -> GND
- C12 pad 1: /NIVARA_BOARD/ANALOG_IN/ESP_4-20_IN -> /NIVARA_BOARD/A_V_OUT/ESP_SEL_VOUT
- C12 pad 2: GND1 -> GND
- C13 pad 1: /NIVARA_BOARD/ANALOG_IN/ESP_A0_32_IN_1 -> /NIVARA_BOARD/A_0-32_IN/A_OUT
- C13 pad 2: GND1 -> GND
- C14 pad 1: /NIVARA_BOARD/ANALOG_IN/ESP_A0_10_IN_1 -> /NIVARA_BOARD/A_0-10_IN/A_V_OUT
- C14 pad 2: GND1 -> GND
- C15 pad 1: /NIVARA_BOARD/A0_V_OUT_1 -> GND
- C15 pad 2: GND1 -> +3.3V
- C16 pad 1: /NIVARA_BOARD/ANALOG_OUT/ESP_SEL_VOUT -> GND
- C16 pad 2: GND1 -> +3.3V
- C17 pad 1: Net-(U13-SET) -> Net-(U19-SET)
- C17 pad 2: GND1 -> GND
- C18 pad 1: Net-(D28-A) -> Net-(D35-A)
- C18 pad 2: GND1 -> GND
- C19 pad 1: Net-(D29-K) -> Net-(D36-K)
- C19 pad 2: GND1 -> GND
- C2 pad 2: GND1 -> GND
- C3 pad 2: GND1 -> GND
- C4 pad 1: +3.3V -> VCC
- C4 pad 2: GND1 -> GND
- C5 pad 1: +3.3V -> Net-(U4-BST)
- C5 pad 2: GND1 -> Net-(U4-SW)
- C6 pad 1: VCC1 -> Net-(U4-FB)
- C6 pad 2: GND1 -> Net-(JP1-A)
- C7 pad 1: Net-(U2-BST) -> Net-(JP1-A)
- C7 pad 2: Net-(U2-SW) -> GND
- C8 pad 1: Net-(U2-FB) -> Net-(JP1-A)
- C8 pad 2: Net-(JP1-A) -> GND
- C9 pad 1: Net-(JP1-A) -> +3.3V
- C9 pad 2: GND1 -> GND
- D1 pad 1: /NIVARA_BOARD/USB_D+ -> VCC
- D1 pad 2: /NIVARA_BOARD/USB_D- -> Net-(D1-A)
- D10 pad 1: /NIVARA_BOARD/NPN_IN/ESP_NPN_IN_2 -> GND
- D11 pad 1: /NIVARA_BOARD/PNP_IN/ESP_PNP_IN_1 -> /NIVARA_BOARD/PNP_IN_1/PNP_OUT
- D12 pad 1: /NIVARA_BOARD/PNP_IN/ESP_PNP_IN_2 -> Net-(D12-K)
- D12 pad 2: Net-(D12-A) -> GND
- D13 pad 1: GND2 -> VCC
- D13 pad 2: Net-(D13-A) -> /NIVARA_BOARD/NPN_OUT_1/NPN_OUT
- D14 pad 1: /NIVARA_BOARD/NPN_OUT_1 -> /NIVARA_BOARD/NPN_OUT_1/NPN_OUT
- D14 pad 2: GND2 -> Net-(D14-A)
- D15 pad 1: GND2 -> /NIVARA_BOARD/PNP_OUT_1
- D15 pad 2: Net-(D15-A) -> GND
- D16 pad 1: /NIVARA_BOARD/NPN_OUT_2 -> GND
- D16 pad 2: GND2 -> Net-(D16-A)
- D17 pad 1: VCC2 -> +3.3V
- D17 pad 2: /NIVARA_BOARD/PNP_OUT_1 -> /NIVARA_BOARD/4-20mA_IN/ESP_4-20_IN
- D18 pad 1: /NIVARA_BOARD/PNP_OUT_1 -> /NIVARA_BOARD/4-20mA_IN/ESP_4-20_IN
- D18 pad 2: Net-(D18-A) -> GND
- D19 pad 1: VCC2 -> /NIVARA_BOARD/A0_V_OUT_1
- D19 pad 2: /NIVARA_BOARD/PNP_OUT_2 -> GND
- D2 pad 1: VCC1 -> /NIVARA_BOARD/USB_D+
- D2 pad 2: GND1 -> /NIVARA_BOARD/USB_D-
- D20 pad 1: /NIVARA_BOARD/PNP_OUT_2 -> /NIVARA_BOARD/D_IN_1/D_OUT
- D21 pad 1: +3.3V -> Net-(D21-K)
- D21 pad 2: /NIVARA_BOARD/ANALOG_IN/ESP_4-20_IN -> GND
- D22 pad 1: /NIVARA_BOARD/ANALOG_IN/ESP_4-20_IN -> VCC
- D22 pad 2: GND1 -> /NIVARA_BOARD/NPN_OUT_2/NPN_OUT
- D23 pad 1: +3.3V -> /NIVARA_BOARD/NPN_OUT_2/NPN_OUT
- D23 pad 2: /NIVARA_BOARD/ANALOG_IN/ESP_A0_32_IN_1 -> Net-(D23-A)
- D24 pad 1: /NIVARA_BOARD/ANALOG_IN/ESP_A0_32_IN_1 -> /NIVARA_BOARD/NPN_IN_2/NPN_OUT
- D24 pad 2: GND1 -> GND
- D25 pad 1: +3.3V -> GND
- D25 pad 2: /NIVARA_BOARD/ANALOG_IN/ESP_A0_10_IN_1 -> Net-(D25-A)
- D26 pad 1: /NIVARA_BOARD/ANALOG_IN/ESP_A0_10_IN_1 -> /NIVARA_BOARD/PNP_IN_2/PNP_OUT
- D26 pad 2: GND1 -> Net-(D26-A)
- D27 pad 1: /NIVARA_BOARD/A0_V_OUT_1 -> /NIVARA_BOARD/PNP_OUT_2
- D27 pad 2: GND1 -> GND
- D28 pad 1: VCC1 -> GND
- D29 pad 1: Net-(D29-K) -> /NIVARA_BOARD/D_IN_2/D_OUT
- D29 pad 2: GND1 -> Net-(D29-A)
- D3 pad 1: VCC2 -> VCC
- D3 pad 2: GND2 -> GND1
- D30 pad 1: /NIVARA_BOARD/I_OUT -> /NIVARA_BOARD/RUN_STOP/D_OUT
- D31 pad 1: /NIVARA_BOARD/D_IN/ESP_D_IN_1 -> +3.3V
- D31 pad 2: Net-(D31-A) -> /NIVARA_BOARD/A_0-32_IN/A_OUT
- D32 pad 1: /NIVARA_BOARD/D_IN/ESP_D_IN_2 -> /NIVARA_BOARD/A_0-32_IN/A_OUT
- D32 pad 2: Net-(D32-A) -> GND
- D33 pad 1: /NIVARA_BOARD/D_IN/ESP_RUN_IN -> +3.3V
- D33 pad 2: Net-(D33-A) -> /NIVARA_BOARD/A_0-10_IN/A_V_OUT
- D4 pad 2: VCC1 -> VCC
- D6 pad 2: GND1 -> GND
- D7 pad 3: GND1 -> GND
- D9 pad 1: /NIVARA_BOARD/NPN_IN/ESP_NPN_IN_1 -> /NIVARA_BOARD/NPN_IN_1/NPN_OUT
- D9 pad 2: Net-(D9-A) -> GND
- F1 pad 2: VCC1 -> VCC
- K1 pad 3: VCC1 -> Net-(U11-1C)
- K1 pad 4: Net-(U14-1C) -> VCC
- K2 pad 3: VCC1 -> VCC
- K2 pad 4: Net-(U14-2C) -> Net-(U11-2C)
- L1 pad 1: Net-(U2-SW) -> Net-(U4-SW)
- Q1 pad 1: Net-(Q1-G) -> Net-(D12-K)
- Q1 pad 2: VCC2 -> GND
- Q1 pad 3: /NIVARA_BOARD/NPN_OUT_1 -> /NIVARA_BOARD/NPN_OUT_1/NPN_OUT
- Q2 pad 2: VCC2 -> VCC
- Q2 pad 3: /NIVARA_BOARD/NPN_OUT_2 -> /NIVARA_BOARD/PNP_OUT_1
- Q3 pad 1: Net-(Q3-G) -> Net-(D21-K)
- Q3 pad 2: GND2 -> GND
- Q3 pad 3: /NIVARA_BOARD/PNP_OUT_1 -> /NIVARA_BOARD/NPN_OUT_2/NPN_OUT
- Q4 pad 2: GND2 -> VCC
- Q5 pad 1: Net-(D28-A) -> Net-(D35-A)
- Q5 pad 3: Net-(D29-K) -> Net-(D36-K)
- R1 pad 1: GND1 -> Net-(U3-GPIO48/SPICLK_N/SUBSPICLK_N_DIFF)
- R1 pad 2: /NIVARA_BOARD/Vbus -> /NIVARA_BOARD/AUX_1
- R10 pad 1: Net-(JP1-A) -> /NIVARA_BOARD/NPN_IN_1/NPN_OUT
- R10 pad 2: Net-(U2-FB) -> Net-(D10-A)
- R11 pad 1: Net-(U2-FB) -> VCC
- R11 pad 2: GND1 -> Net-(R11-Pad2)
- R12 pad 1: GND1 -> +3.3V
- R12 pad 2: Net-(D5-K) -> Net-(D11-A)
- R13 pad 1: Net-(D7-A1) -> /NIVARA_BOARD/NPN_OUT_1
- R13 pad 2: /NIVARA_BOARD/RS485_A -> Net-(R13-Pad2)
- R14 pad 1: Net-(D7-A2) -> Net-(D12-K)
- R14 pad 2: /NIVARA_BOARD/RS485_B -> GND
- R15 pad 1: VCC2 -> VCC
- R16 pad 1: +3.3V -> VCC
- R16 pad 2: Net-(D9-A) -> Net-(D14-A)
- R17 pad 1: VCC2 -> +3.3V
- R18 pad 1: +3.3V -> Net-(Q2-G)
- R18 pad 2: Net-(D10-A) -> Net-(R18-Pad2)
- R19 pad 1: /NIVARA_BOARD/PNP_IN_1 -> VCC
- R19 pad 2: Net-(R19-Pad2) -> Net-(Q2-G)
- R2 pad 1: /NIVARA_BOARD/Vbus -> Net-(U3-GPIO45)
- R2 pad 2: Net-(R2-Pad2) -> /NIVARA_BOARD/AUX_2
- R20 pad 1: +3.3V -> /NIVARA_BOARD/PNP_OUT_1
- R20 pad 2: Net-(D11-A) -> Net-(D16-A)
- R21 pad 1: /NIVARA_BOARD/PNP_IN_2 -> /NIVARA_BOARD/4-20mA_IN/ESP_4-20_IN
- R21 pad 2: Net-(R21-Pad2) -> /NIVARA_BOARD/A4_20_IN_1
- R22 pad 1: +3.3V -> /NIVARA_BOARD/A4_20_IN_1
- R22 pad 2: Net-(D12-A) -> GND
- R23 pad 1: /NIVARA_BOARD/NPN_OUT/ESP_NPN_OUT_1 -> +3.3V
- R23 pad 2: Net-(R23-Pad2) -> /NIVARA_BOARD/A_V_OUT/SDA_V
- R24 pad 1: Net-(Q1-G) -> +3.3V
- R24 pad 2: Net-(R24-Pad2) -> /NIVARA_BOARD/A_V_OUT/SCLK_V
- R25 pad 1: VCC2 -> Net-(U10-SEL)
- R25 pad 2: Net-(Q1-G) -> /NIVARA_BOARD/A_V_OUT/ESP_SEL_VOUT
- R26 pad 1: /NIVARA_BOARD/NPN_OUT_1 -> +3.3V
- R26 pad 2: Net-(D13-A) -> /NIVARA_BOARD/A_V_OUT/ESP_SEL_VOUT
- R27 pad 1: /NIVARA_BOARD/NPN_OUT/ESP_NPN_OUT_2 -> /NIVARA_BOARD/D_IN_1
- R28 pad 1: Net-(Q2-G) -> +3.3V
- R28 pad 2: Net-(R28-Pad2) -> Net-(D20-A)
- R29 pad 1: VCC2 -> /NIVARA_BOARD/NPN_OUT_2
- R29 pad 2: Net-(Q2-G) -> Net-(R29-Pad2)
- R3 pad 1: Net-(U30-CC2) -> GND
- R3 pad 2: GND1 -> Net-(D4-K)
- R30 pad 1: /NIVARA_BOARD/NPN_OUT_2 -> Net-(D21-K)
- R30 pad 2: Net-(D15-A) -> GND
- R31 pad 1: /NIVARA_BOARD/PNP_OUT/ESP_PNP_OUT_1 -> VCC
- R32 pad 1: Net-(Q3-G) -> VCC
- R32 pad 2: VCC2 -> Net-(D23-A)
- R33 pad 1: GND2 -> /NIVARA_BOARD/NPN_IN_2
- R33 pad 2: Net-(Q3-G) -> Net-(R33-Pad2)
- R34 pad 1: VCC2 -> /NIVARA_BOARD/NPN_IN_2/NPN_OUT
- R34 pad 2: Net-(D18-A) -> Net-(D25-A)
- R35 pad 1: /NIVARA_BOARD/PNP_OUT/ESP_PNP_OUT_2 -> VCC
- R36 pad 1: Net-(Q4-G) -> +3.3V
- R36 pad 2: VCC2 -> Net-(D26-A)
- R37 pad 1: GND2 -> +3.3V
- R37 pad 2: Net-(Q4-G) -> Net-(R37-Pad2)
- R38 pad 1: VCC2 -> Net-(Q4-G)
- R38 pad 2: Net-(D20-A) -> Net-(R38-Pad2)
- R39 pad 1: /NIVARA_BOARD/ANALOG_IN/ESP_4-20_IN -> VCC
- R39 pad 2: /NIVARA_BOARD/A4_20_IN_1 -> Net-(Q4-G)
- R4 pad 1: Net-(U30-CC1) -> Net-(JP1-A)
- R4 pad 2: GND1 -> Net-(U4-FB)
- R40 pad 1: /NIVARA_BOARD/A4_20_IN_1 -> /NIVARA_BOARD/PNP_OUT_2
- R40 pad 2: GND1 -> Net-(D28-A)
- R41 pad 1: /NIVARA_BOARD/ANALOG_IN/ESP_A0_32_IN_1 -> /NIVARA_BOARD/D_IN_2
- R41 pad 2: /NIVARA_BOARD/A0_32_IN_1 -> Net-(R41-Pad2)
- R42 pad 1: GND1 -> +3.3V
- R42 pad 2: /NIVARA_BOARD/ANALOG_IN/ESP_A0_32_IN_1 -> Net-(D29-A)
- R43 pad 1: /NIVARA_BOARD/ANALOG_IN/ESP_A0_10_IN_1 -> /NIVARA_BOARD/RUN/STOP
- R43 pad 2: /NIVARA_BOARD/A0_10_IN_1 -> Net-(R43-Pad2)
- R44 pad 1: GND1 -> +3.3V
- R44 pad 2: /NIVARA_BOARD/ANALOG_IN/ESP_A0_10_IN_1 -> Net-(D30-A)
- R45 pad 1: +3.3V -> /NIVARA_BOARD/A_0-32_IN/A_OUT
- R45 pad 2: /NIVARA_BOARD/ANALOG_OUT/SDA_V -> /NIVARA_BOARD/A0_32_IN_1
- R46 pad 1: +3.3V -> GND
- R46 pad 2: /NIVARA_BOARD/ANALOG_OUT/SCLK_V -> /NIVARA_BOARD/A_0-32_IN/A_OUT
- R47 pad 1: Net-(U12-SEL) -> /NIVARA_BOARD/A_0-10_IN/A_V_OUT
- R47 pad 2: /NIVARA_BOARD/ANALOG_OUT/ESP_SEL_VOUT -> /NIVARA_BOARD/A_0-10_IN/A_V_IN
- R48 pad 1: +3.3V -> GND
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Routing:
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- removed copper zone on F.Cu, net +3.3V
- removed copper zone on In1.Cu, net GND1
- removed copper zone on B.Cu, net GND2
- removed copper zone on In2.Cu, net VCC2

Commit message: Changes en diseño.
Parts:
- moved P4 59.9 mm to (158.4, 49.5)
- moved CN1 56.5 mm to (173.7, 50.1), turned to 180 degrees
- moved P5 51.2 mm to (145.0, 123.9), turned to 180 degrees
- moved P3 46.5 mm to (148.2, 49.5)
- moved P6 42.3 mm to (155.3, 123.7), turned to 180 degrees
- moved J1 34.1 mm to (138.5, 100.7)
- moved P2 33.9 mm to (137.9, 49.5)
- moved CN2 30.2 mm to (175.5, 123.5), turned to 180 degrees
- moved U1 27.0 mm to (191.5, 85.0)
- moved P1 23.8 mm to (127.7, 49.5)
- moved U2 8.46 mm to (117.4, 49.5)
- moved P7 4.70 mm to (116.7, 123.2)
- moved P8 4.20 mm to (132.2, 123.2)

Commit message: cAMBIOS EN EL PCB Y ESQUEMA.
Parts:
- moved R9 265.4 mm to (192.0, 51.0)
- moved D9 261.8 mm to (189.5, 55.5), turned to 90 degrees
- moved D10 260.6 mm to (188.0, 60.0), turned to -90 degrees
- moved R10 259.0 mm to (190.0, 60.0), turned to -90 degrees
- moved U6 256.4 mm to (193.5, 56.5), turned to -90 degrees
- moved K2 240.6 mm to (235.5, 103.3), turned to -90 degrees
- moved K1 239.6 mm to (250.5, 103.4), turned to -90 degrees
- moved U11 233.0 mm to (242.9, 91.7)
- moved D3 225.1 mm to (170.5, 47.9), turned to 90 degrees
- moved C15 205.3 mm to (78.3, 124.5)
- moved C16 205.3 mm to (67.8, 124.5)
- moved C19 205.3 mm to (71.9, 105.1)
- moved D15 205.3 mm to (121.0, 115.1)
- moved D20 205.3 mm to (130.7, 34.8)
- moved D24 205.3 mm to (129.6, 65.3)
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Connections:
- net /NIVARA_BOARD/A_OUT_1 renamed /NIVARA_BOARD/A_OUT
- net Net-(F1-Pad1) renamed /VIN
- net Net-(JP1-A) renamed /NIVARA_BOARD/PowerSupply/VOUT
- net Net-(U4-BST) renamed /NIVARA_BOARD/PowerSupply/BST
- net Net-(U4-FB) renamed /NIVARA_BOARD/PowerSupply/FB
- net Net-(U4-SW) renamed /NIVARA_BOARD/PowerSupply/SW
- D3 pad 2: GND1 -> GND
- H1 pad 1: GND1 -> GND
- H2 pad 1: GND1 -> GND
- K1 pad 1: /NIVARA_BOARD/RLY_1_NC -> /NIVARA_BOARD/RLY_1_NO
- K1 pad 2: /NIVARA_BOARD/RLY_1_NO -> /NIVARA_BOARD/RLY_1_NC
- K1 pad 3: Net-(U11-1C) -> VCC
- K1 pad 4: VCC -> Net-(U11-1C)
- K2 pad 1: /NIVARA_BOARD/RLY_2_NC -> /NIVARA_BOARD/RLY_2_NO
- K2 pad 2: /NIVARA_BOARD/RLY_2_NO -> /NIVARA_BOARD/RLY_2_NC
- K2 pad 3: VCC -> Net-(U11-2C)
- K2 pad 4: Net-(U11-2C) -> VCC
- U2 pad 2: GND1 -> GND
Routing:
- net VCC: track 0.00 -> 30.8 mm
- net /NIVARA_BOARD/RLY_2_C: track 0.00 -> 21.2 mm
- net /NIVARA_BOARD/RLY_1_C: track 0.00 -> 21.1 mm
- net /NIVARA_BOARD/RLY_2_NO: track 0.00 -> 8.49 mm
- net /NIVARA_BOARD/RLY_2_NC: track 0.00 -> 8.49 mm
- net /NIVARA_BOARD/RLY_1_NO: track 0.00 -> 8.41 mm
- net /NIVARA_BOARD/RLY_1_NC: track 0.00 -> 8.41 mm
- net Net-(U11-1C): track 0.00 -> 7.51 mm
- net /NIVARA_BOARD/NPN_IN_1: track 0.00 -> 7.48 mm
- net Net-(U11-2C): track 0.00 -> 7.31 mm
- net /NIVARA_BOARD/NPN_IN_1/NPN_OUT: track 0.00 -> 5.64 mm
- net Net-(D5-K): track 0.00 -> 5.45 mm
- net Net-(R9-Pad2): track 0.00 -> 3.55 mm
- net Net-(D4-K): track 0.00 -> 2.93 mm
- net Net-(D10-A): track 0.00 -> 2.02 mm
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- added copper zone on F.Cu, net +3.3V
- added copper zone on F.Cu, net /NIVARA_BOARD/PowerSupply/BST
- added copper zone on F.Cu, net /NIVARA_BOARD/PowerSupply/FB
- added copper zone on F.Cu, net /NIVARA_BOARD/PowerSupply/SW
- added copper zone on F.Cu, net /NIVARA_BOARD/PowerSupply/VOUT
- added copper zone on F.Cu, net /VIN
- added copper zone on F.Cu, net GND
- added copper zone on In1.Cu, net GND
- added copper zone on F.Cu, net VCC
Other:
- outline, holes or cut-outs redrawn
